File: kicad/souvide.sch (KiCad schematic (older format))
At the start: 12 parts, among them Q1 J6 NPN

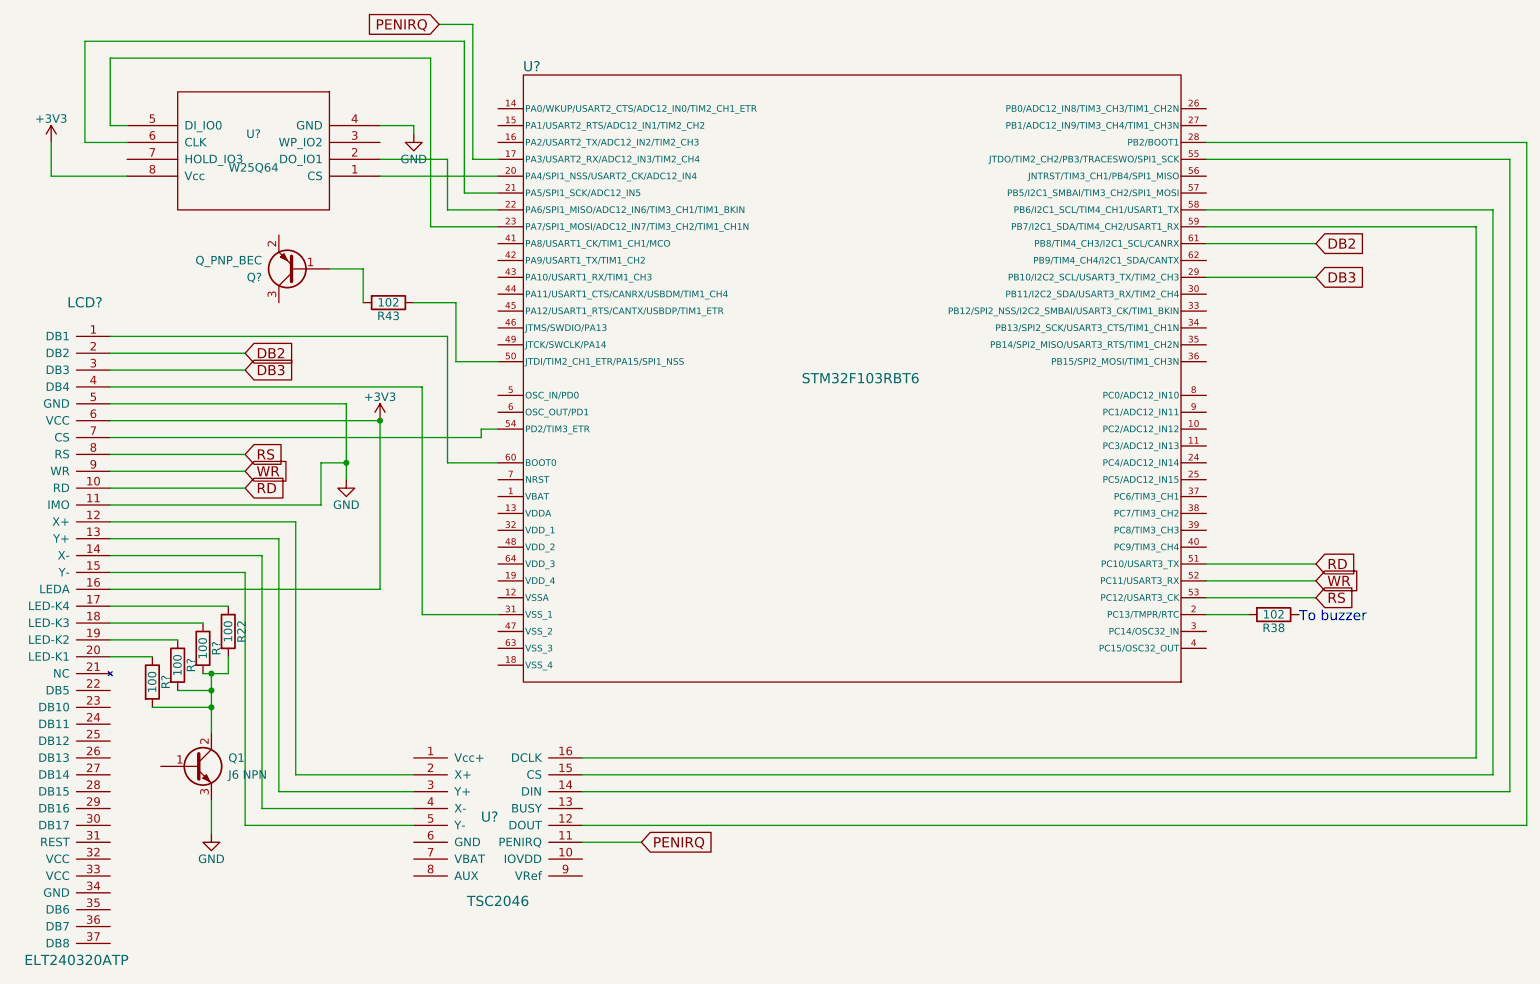
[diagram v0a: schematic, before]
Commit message: Fix display connection in electric schema
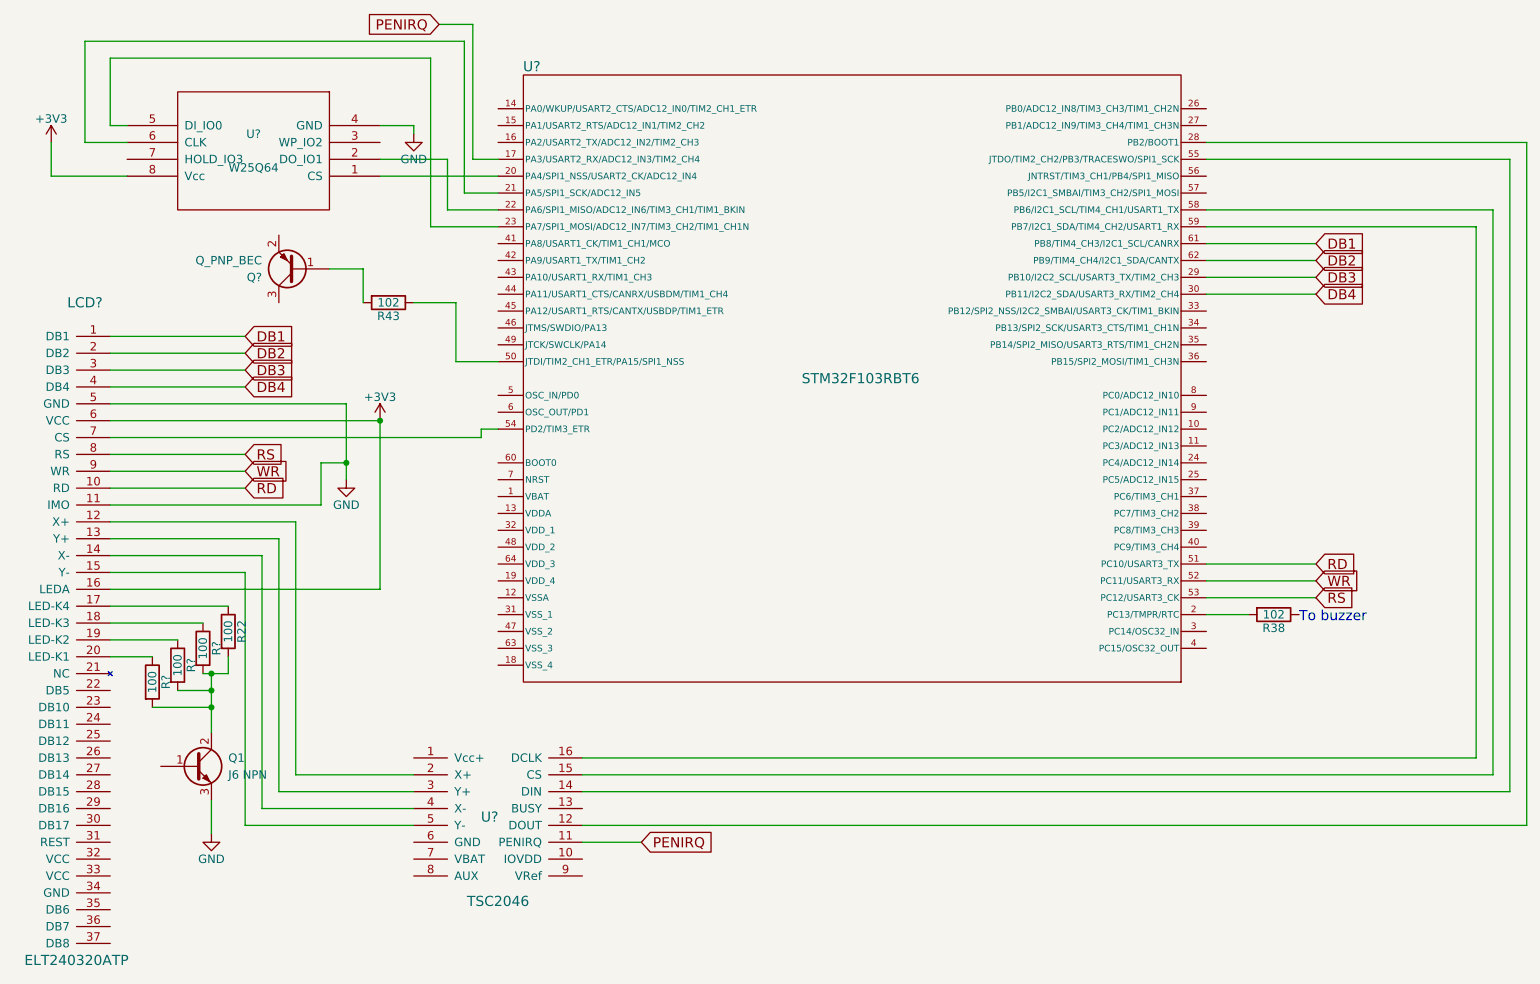
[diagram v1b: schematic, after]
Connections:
- net DB2: now also U?.62 (PB9/TIM4_CH4/I2C1_SDA/CANTX); no longer U?.61 (PB8/TIM4_CH3/I2C1_SCL/CANRX)
- net DB4: now reaches U?.30 (PB11/I2C2_SDA/USART3_RX/TIM2_CH4)
- net DB4: now also LCD?.4 (DB4)
- net at U?.31 (VSS_1): no longer LCD?.4 (DB4)
- net at U?.60 (BOOT0): no longer LCD?.1 (DB1)
- new net DB1: LCD?.1 (DB1), U?.61 (PB8/TIM4_CH3/I2C1_SCL/CANRX)
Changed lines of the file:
@@
 LIBS:elt240320atp
 LIBS:tsc2046
+LIBS:souvide-cache
 EELAYER 25 0
 EELAYER END
@@
 Wire Wire Line
 	2900 2000 2900 2050
-Wire Wire Line
-	3400 4000 3100 4000
-Wire Wire Line
-	3100 4000 3100 3250
-Wire Wire Line
-	3100 3250 1100 3250
-Text GLabel 8250 2700 2    60   Input ~ 0
+Text GLabel 8250 2800 2    60   Input ~ 0
 DB2
 Wire Wire Line
-	7600 2700 8250 2700
+	7600 2800 8250 2800
 Text GLabel 1900 3350 2    60   Input ~ 0
 DB2
@@
 Wire Wire Line
 	8250 2900 7600 2900
-Wire Wire Line
-	2950 4900 3400 4900
-Wire Wire Line
-	2950 4900 2950 3550
-Wire Wire Line
-	2950 3550 1100 3550
 Wire Wire Line
 	3400 3800 3300 3800
@@
 Wire Wire Line
 	2600 2850 2400 2850
+Text GLabel 1900 3250 2    60   Input ~ 0
+DB1
+Wire Wire Line
+	1100 3250 1900 3250
+Text GLabel 8250 2700 2    60   Input ~ 0
+DB1
+Wire Wire Line
+	7600 2700 8250 2700
+Text GLabel 8250 3000 2    60   Input ~ 0
+DB4
+Wire Wire Line
+	7600 3000 8250 3000
+Text GLabel 1900 3550 2    60   Input ~ 0
+DB4
+Wire Wire Line
+	1100 3550 1900 3550
 $EndSCHEMATC
